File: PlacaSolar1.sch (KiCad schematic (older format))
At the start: 32 parts, among them J1 Jack-DC, J2 Conn_01x03_Female, J3 Conn_01x06_Female, J4 Conn_01x15_Female, J5 Conn_01x15_Female, SW1 SW_SPDT, SW2 SW_Push, U1 L78L05_SO8

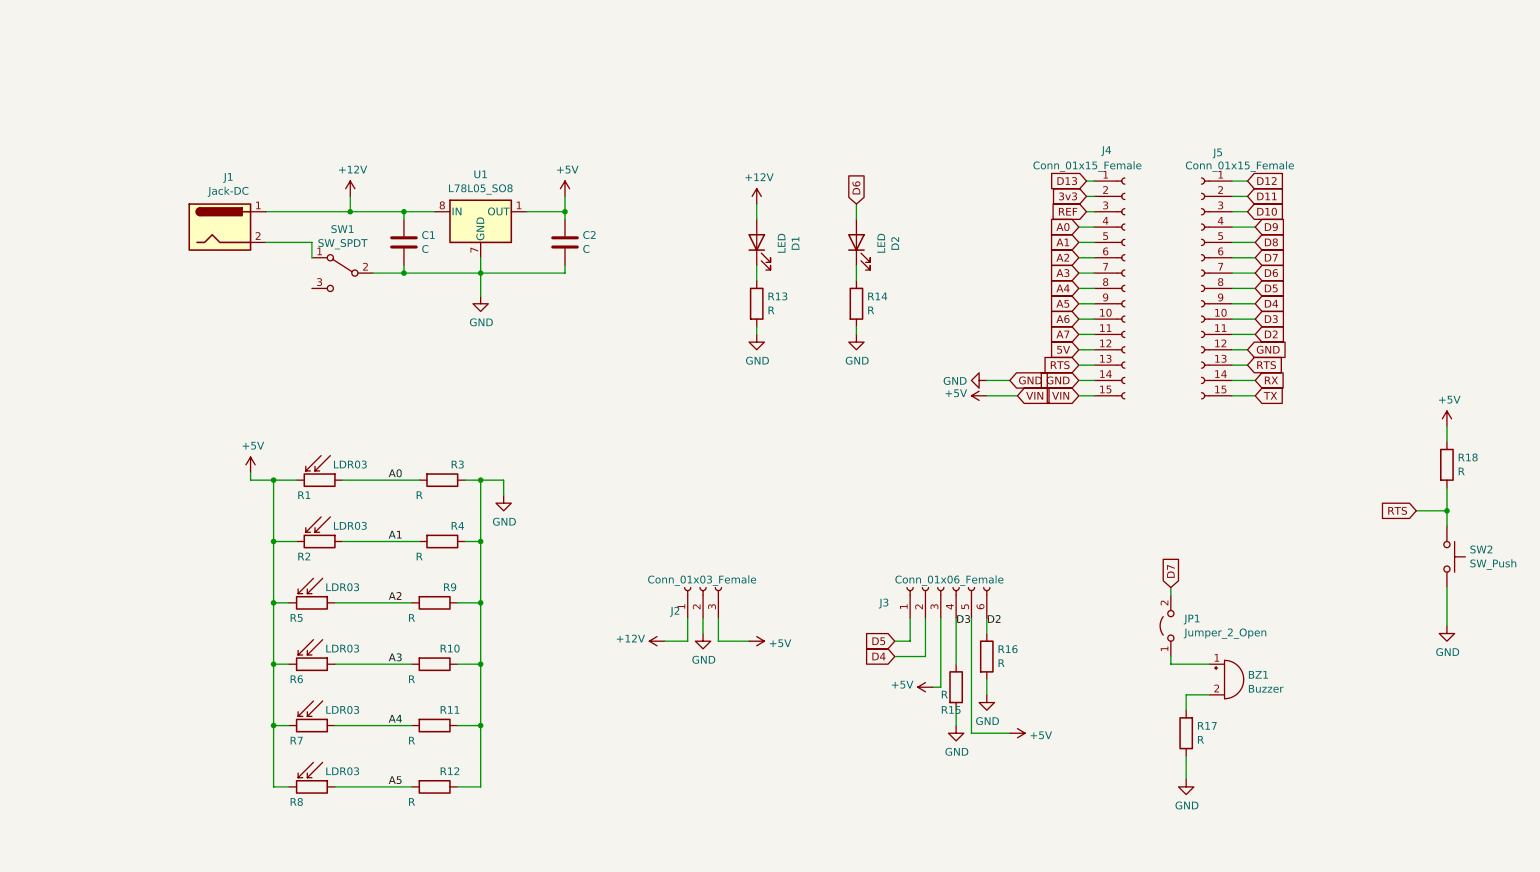
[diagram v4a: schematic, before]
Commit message: Corrigindo footprint do interruptor e adicionando alguns modelos 3d
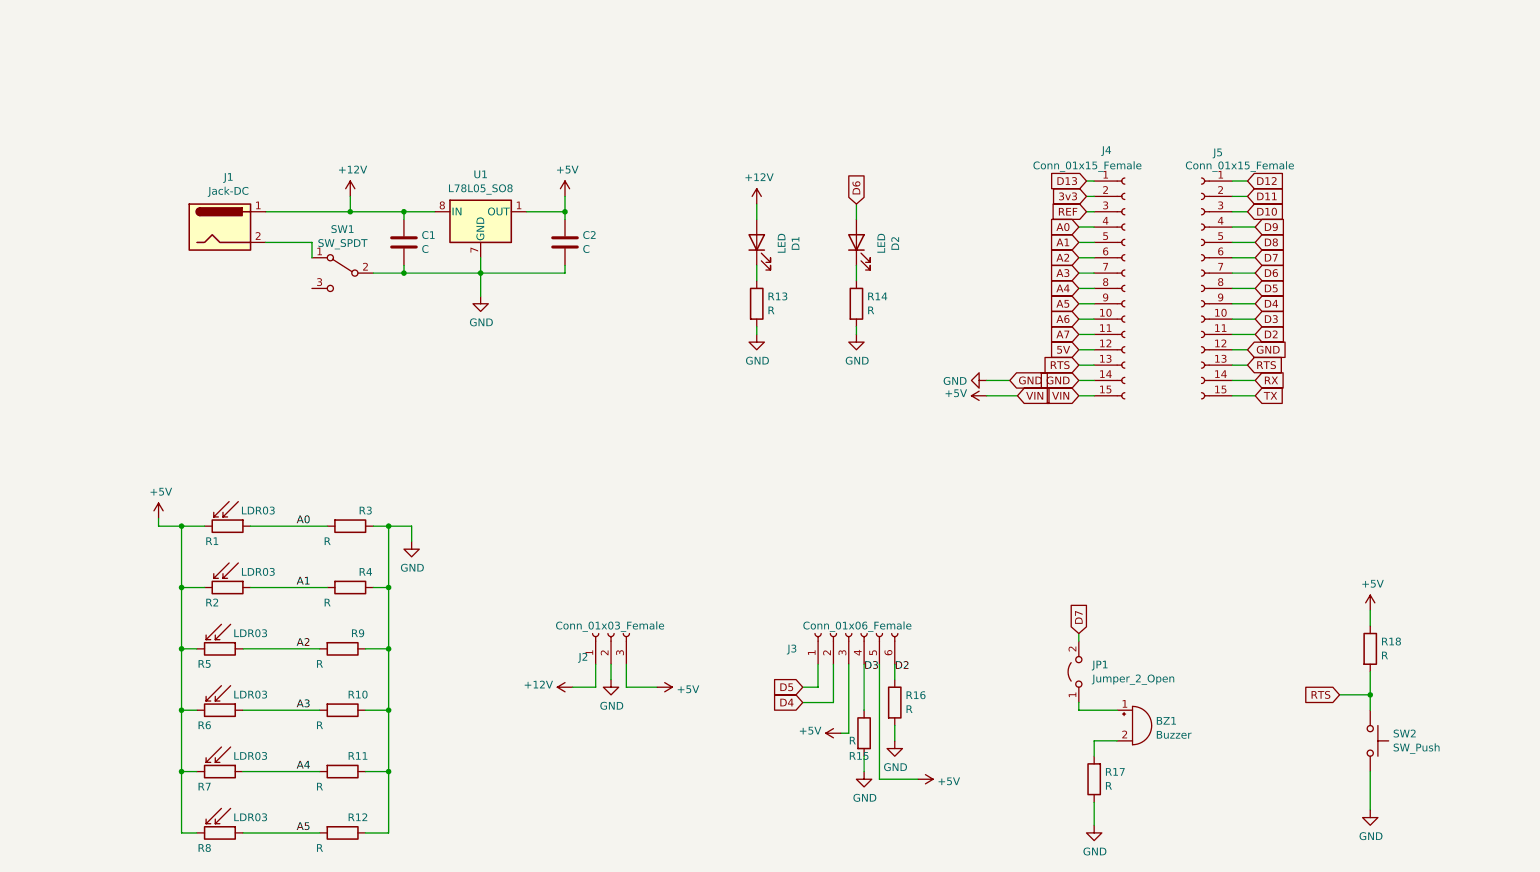
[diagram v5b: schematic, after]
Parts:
- SW1: footprint 2267077-2:TE_2267077-2 -> TE_2267077-2:TE_2267077-2
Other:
- moved on the sheet: BZ1, J2, J3, JP1, R1, R10, R11, R12, R15, R16, R17, R18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

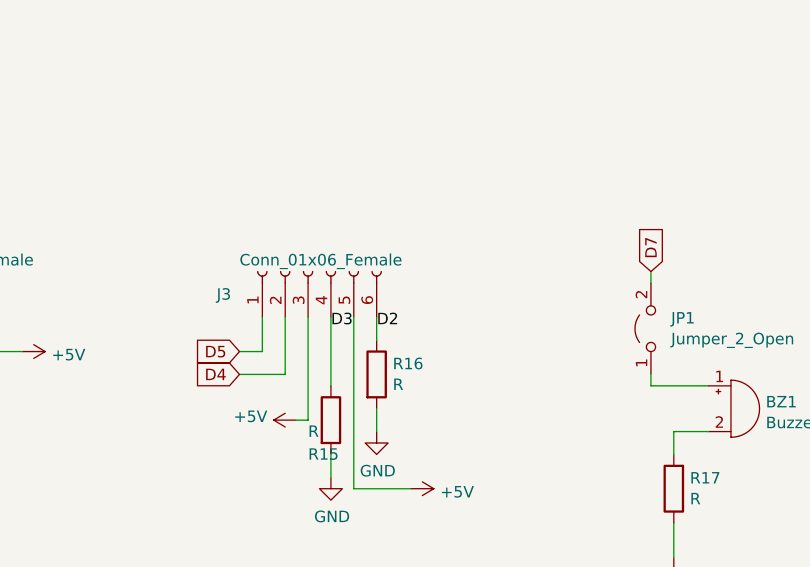
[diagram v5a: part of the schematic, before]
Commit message: Adicionando modelos 3d, falta o modelo dos bornes, inicio da PCB
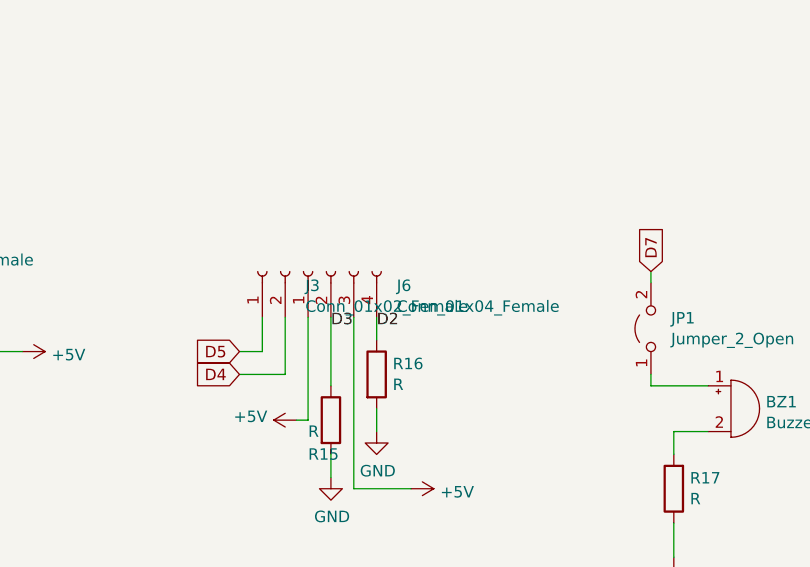
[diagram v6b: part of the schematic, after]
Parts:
- removed J3: Conn_01x06_Female, TerminalBlock:TerminalBlock_bornier-6_P5.08mm, symbol Connector:Conn_01x06_Female
- added J3: Conn_01x02_Female, TerminalBlock:TerminalBlock_bornier-2_P5.08mm, symbol Connector:Conn_01x02_Female
- added J6: Conn_01x04_Female, TerminalBlock:TerminalBlock_bornier-4_P5.08mm, symbol Connector:Conn_01x04_Female
- R2: footprint TerminalBlock:TerminalBlock_bornier-3_P5.08mm -> TerminalBlock:TerminalBlock_bornier-2_P5.08mm
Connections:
- net +5V: now also J6.1 (Pin_1), J6.3 (Pin_3)
- net D2: now also J6.4 (Pin_4)
- net D3: now also J6.2 (Pin_2)
- net D4: now also J3.2 (Pin_2)
- net D5: now also J3.1 (Pin_1)
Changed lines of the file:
@@
-	0    -1   -1   0
-$EndComp
-$Comp
-L Connector:Conn_01x06_Female J3
-U 1 1 61522486
-P 6150 4500
-F 0 "J3" V 6050 4900 50  0000 R CNN
-F 1 "Conn_01x06_Female" V 6200 4800 50  0000 R CNN
-F 2 "TerminalBlock:TerminalBlock_bornier-6_P5.08mm" H 6150 4500 50  0001 C CNN
-F 3 "~" H 6150 4500 50  0001 C CNN
-	1    6150 4500
 	0    -1   -1   0
 $EndComp
@@
 F 0 "R2" V 2200 4100 50  0000 C CNN
 F 1 "LDR03" V 2000 4400 50  0000 C CNN
-F 2 "TerminalBlock:TerminalBlock_bornier-3_P5.08mm" V 2275 4200 50  0001 C CNN
+F 2 "TerminalBlock:TerminalBlock_bornier-2_P5.08mm" V 2275 4200 50  0001 C CNN
 F 3 "http://www.elektronica-componenten.nl/WebRoot/StoreNL/Shops/61422969/54F1/BA0C/C664/31B9/2173/C0A8/2AB9/2AEF/LDR03IMP.pdf" H 2100 4150 50  0001 C CNN
 	1    2100 4200
@@
 Wire Wire Line
 	9550 4900 9550 4750
+$Comp
+L Connector:Conn_01x04_Female J6
+U 1 1 61473C9D
+P 6250 4500
+F 0 "J6" V 6188 4212 50  0000 R CNN
+F 1 "Conn_01x04_Female" V 6097 4212 50  0000 R CNN
+F 2 "TerminalBlock:TerminalBlock_bornier-4_P5.08mm" H 6250 4500 50  0001 C CNN
+F 3 "~" H 6250 4500 50  0001 C CNN
+	1    6250 4500
+	0    -1   -1   0
+$EndComp
+$Comp
+L Connector:Conn_01x02_Female J3
+U 1 1 61474DE5
+P 5950 4500
+F 0 "J3" V 5888 4312 50  0000 R CNN
+F 1 "Conn_01x02_Female" V 5797 4312 50  0000 R CNN
+F 2 "TerminalBlock:TerminalBlock_bornier-2_P5.08mm" H 5950 4500 50  0001 C CNN
+F 3 "~" H 5950 4500 50  0001 C CNN
+	1    5950 4500
+	0    -1   -1   0
+$EndComp
 $EndSCHEMATC

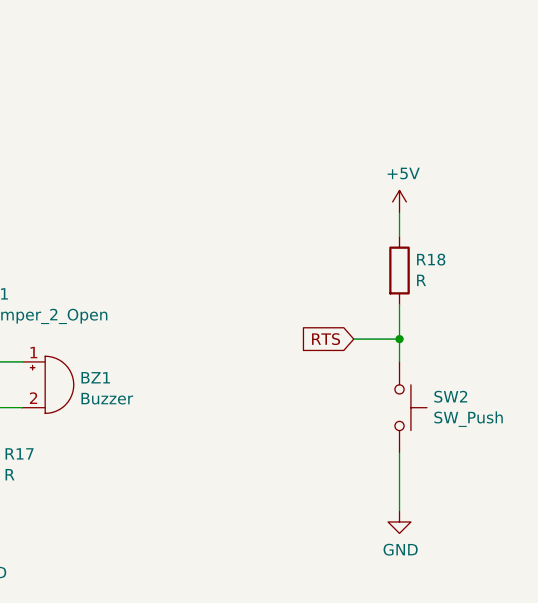
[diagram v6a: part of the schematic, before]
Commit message: Removendo botão de Reset
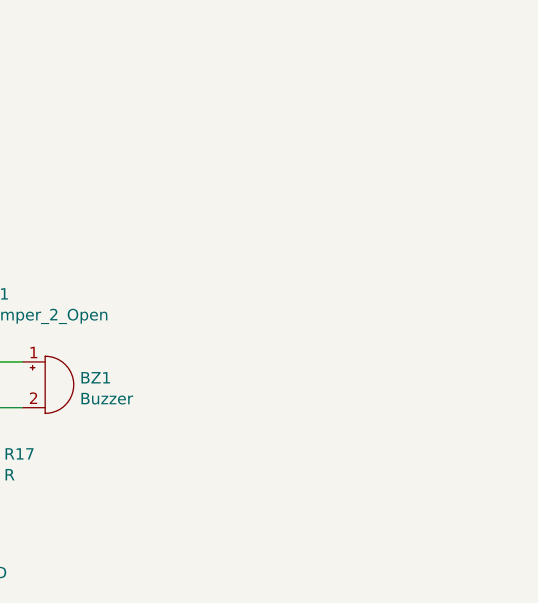
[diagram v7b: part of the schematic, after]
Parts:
- removed R18: R, Resistor_THT:R_Axial_DIN0207_L6.3mm_D2.5mm_P10.16mm_Horizontal, symbol Device:R
- removed SW2: SW_Push, Button_Switch_THT:SW_PUSH_6mm, symbol Switch:SW_Push
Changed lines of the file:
@@
 $EndComp
-$Comp
-L Switch:SW_Push SW2
-U 1 1 613C8742
-P 9550 5200
-F 0 "SW2" V 9504 5348 50  0000 L CNN
-F 1 "SW_Push" V 9595 5348 50  0000 L CNN
-F 2 "Button_Switch_THT:SW_PUSH_6mm" H 9550 5400 50  0001 C CNN
-F 3 "~" H 9550 5400 50  0001 C CNN
-	1    9550 5200
-	0    1    1    0
-$EndComp
-$Comp
-L power:+5V #PWR019
-U 1 1 613CCD35
-P 9550 4350
-F 0 "#PWR019" H 9550 4200 50  0001 C CNN
-F 1 "+5V" H 9565 4523 50  0000 C CNN
-F 2 "" H 9550 4350 50  0001 C CNN
-F 3 "" H 9550 4350 50  0001 C CNN
-	1    9550 4350
-	1    0    0    -1
-$EndComp
-$Comp
-L power:GND #PWR020
-U 1 1 613CD321
-P 9550 5650
-F 0 "#PWR020" H 9550 5400 50  0001 C CNN
-F 1 "GND" H 9555 5477 50  0000 C CNN
-F 2 "" H 9550 5650 50  0001 C CNN
-F 3 "" H 9550 5650 50  0001 C CNN
-	1    9550 5650
-	1    0    0    -1
-$EndComp
-$Comp
-L Device:R R18
-U 1 1 613D230B
-P 9550 4600
-F 0 "R18" H 9620 4646 50  0000 L CNN
-F 1 "R" H 9620 4555 50  0000 L CNN
-F 2 "Resistor_THT:R_Axial_DIN0207_L6.3mm_D2.5mm_P10.16mm_Horizontal" V 9480 4600 50  0001 C CNN
-F 3 "~" H 9550 4600 50  0001 C CNN
-	1    9550 4600
-	1    0    0    -1
-$EndComp
-Wire Wire Line
-	9550 5000 9550 4900
-Text GLabel 9350 4900 0    50   Input ~ 0
-RTS
-Wire Wire Line
-	9550 4450 9550 4350
-Wire Wire Line
-	9550 5400 9550 5650
-Wire Wire Line
-	9550 4900 9350 4900
-Connection ~ 9550 4900
-Wire Wire Line
-	9550 4900 9550 4750
 $Comp
 L Connector:Conn_01x04_Female J6

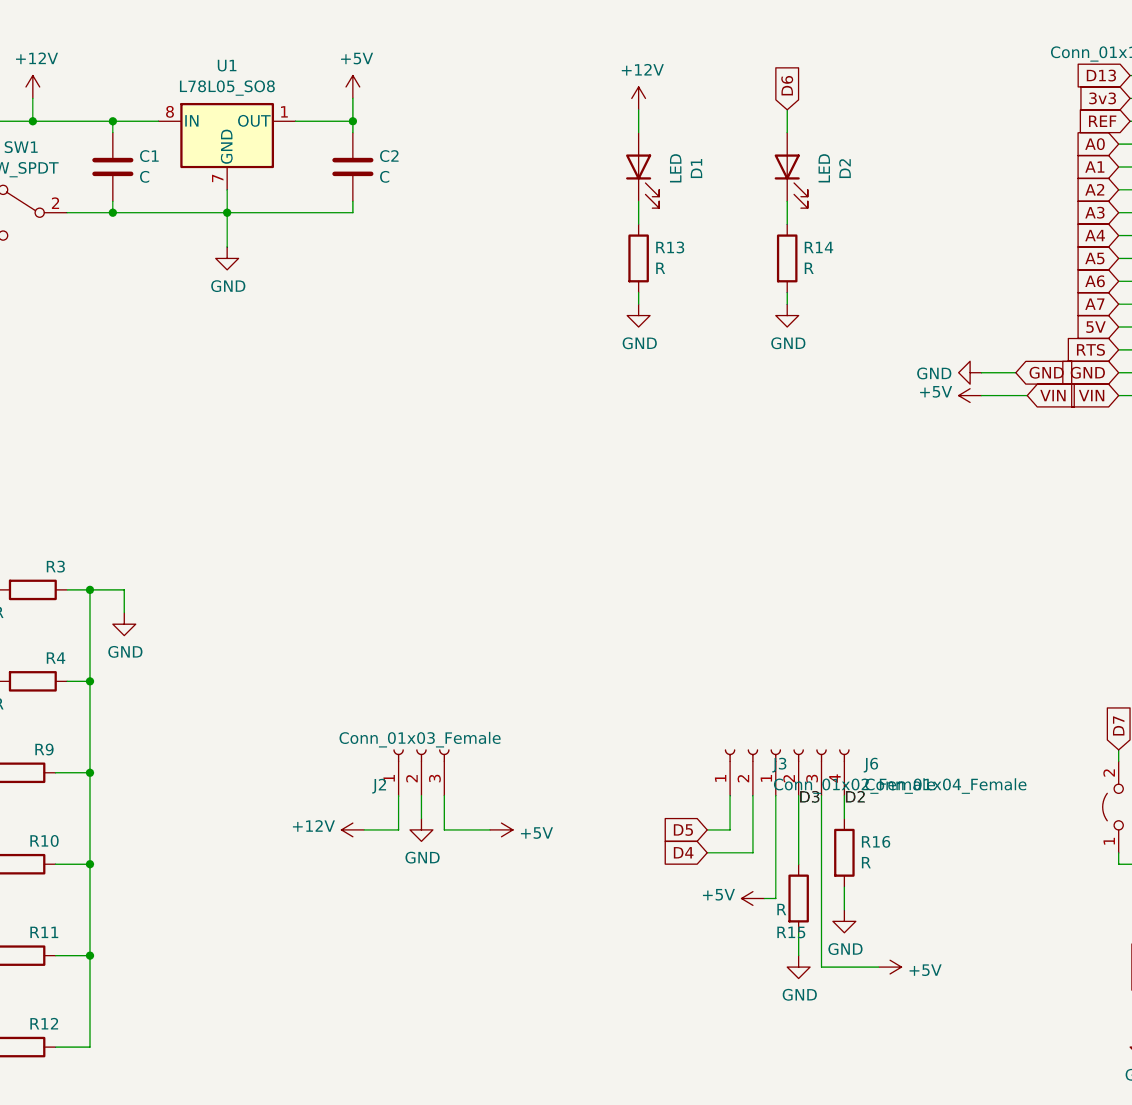
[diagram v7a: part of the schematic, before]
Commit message: Primeira versão de trilhas da PCB, falta verificar o tamanho de certos componentes
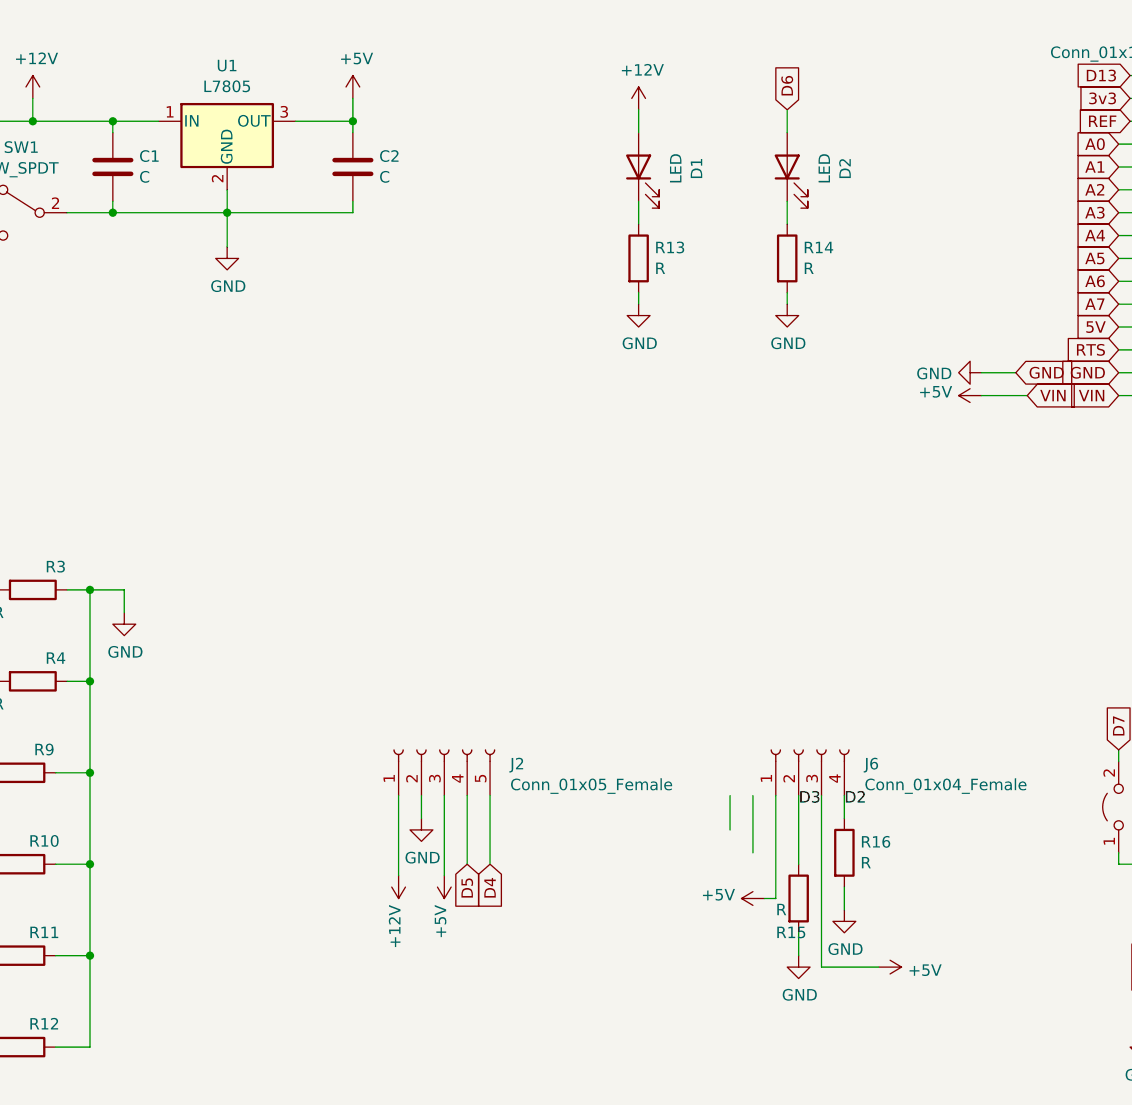
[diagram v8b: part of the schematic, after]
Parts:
- removed J2: Conn_01x03_Female, TerminalBlock:TerminalBlock_bornier-3_P5.08mm, symbol Connector:Conn_01x03_Female
- removed J3: Conn_01x02_Female, TerminalBlock:TerminalBlock_bornier-2_P5.08mm, symbol Connector:Conn_01x02_Female
- removed U1: L78L05_SO8, Package_TO_SOT_THT:TO-220-3_Vertical, symbol Regulator_Linear:L78L05_SO8
- added J2: Conn_01x05_Female, Connector_PinHeader_2.54mm:PinHeader_1x05_P2.54mm_Vertical, symbol Connector:Conn_01x05_Female
- added U1: L7805, Package_TO_SOT_THT:TO-220-3_Vertical, symbol Regulator_Linear:L7805
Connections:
- wire segments 110 -> 108
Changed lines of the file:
@@
-	1    0    0    -1
-$EndComp
-$Comp
-L Regulator_Linear:L78L05_SO8 U1
-U 1 1 613A917B
-P 3750 1750
-F 0 "U1" H 3750 1992 50  0000 C CNN
-F 1 "L78L05_SO8" H 3750 1901 50  0000 C CNN
-F 2 "Package_TO_SOT_THT:TO-220-3_Vertical" H 3850 1950 50  0001 C CIN
-F 3 "http://www.st.com/content/ccc/resource/technical/document/datasheet/15/55/e5/aa/23/5b/43/fd/CD00000446.pdf/files/CD00000446.pdf/jcr:content/translations/en.CD00000446.pdf" H 3950 1750 50  0001 C CNN
-	1    3750 1750
 	1    0    0    -1
 $EndComp
@@
 	6050 4700 6050 4950
 Wire Wire Line
-	5850 4950 6050 4950
-Wire Wire Line
 	5950 4700 5950 4850
-Wire Wire Line
-	5850 4850 5950 4850
-Text GLabel 5850 4950 0    50   Input ~ 0
+Text GLabel 4900 5000 3    50   Input ~ 0
 D4
-Text GLabel 5850 4850 0    50   Input ~ 0
+Text GLabel 4800 5000 3    50   Input ~ 0
 D5
-$Comp
-L Connector:Conn_01x03_Female J2
-U 1 1 613F1034
-P 4600 4500
-F 0 "J2" V 4446 4648 50  0000 L CNN
-F 1 "Conn_01x03_Female" V 4650 4150 50  0000 L CNN
-F 2 "TerminalBlock:TerminalBlock_bornier-3_P5.08mm" H 4600 4500 50  0001 C CNN
-F 3 "~" H 4600 4500 50  0001 C CNN
-	1    4600 4500
-	0    -1   -1   0
-$EndComp
 $Comp
 L power:GND #PWR07
@@
 	1    0    0    -1
 $EndComp
-Wire Wire Line
-	4600 4800 4600 4700
 $Comp
 L power:+12V #PWR06
 U 1 1 613F8720
-P 4350 4850
-F 0 "#PWR06" H 4350 4700 50  0001 C CNN
-F 1 "+12V" V 4365 4978 50  0000 L CNN
-F 2 "" H 4350 4850 50  0001 C CNN
-F 3 "" H 4350 4850 50  0001 C CNN
-	1    4350 4850
-	0    -1   -1   0
-$EndComp
-Wire Wire Line
-	4500 4700 4500 4850
-Wire Wire Line
-	4500 4850 4350 4850
+P 4500 5050
+F 0 "#PWR06" H 4500 4900 50  0001 C CNN
+F 1 "+12V" V 4515 5178 50  0000 L CNN
+F 2 "" H 4500 5050 50  0001 C CNN
+F 3 "" H 4500 5050 50  0001 C CNN
+	1    4500 5050
+	-1   0    0    1
+$EndComp
 $Comp
 L power:+5V #PWR08
 U 1 1 613FB42D
-P 4900 4850
-F 0 "#PWR08" H 4900 4700 50  0001 C CNN
-F 1 "+5V" V 4915 4978 50  0000 L CNN
-F 2 "" H 4900 4850 50  0001 C CNN
-F 3 "" H 4900 4850 50  0001 C CNN
-	1    4900 4850
-	0    1    1    0
-$EndComp
-Wire Wire Line
-	4900 4850 4700 4850
-Wire Wire Line
-	4700 4850 4700 4700
+P 4700 5050
+F 0 "#PWR08" H 4700 4900 50  0001 C CNN
+F 1 "+5V" V 4715 5178 50  0000 L CNN
+F 2 "" H 4700 5050 50  0001 C CNN
+F 3 "" H 4700 5050 50  0001 C CNN
+	1    4700 5050
+	-1   0    0    1
+$EndComp
 $Comp
 L Sensor_Optical:LDR03 R1
@@
 	0    -1   -1   0
 $EndComp
-$Comp
-L Connector:Conn_01x02_Female J3
-U 1 1 61474DE5
-P 5950 4500
-F 0 "J3" V 5888 4312 50  0000 R CNN
-F 1 "Conn_01x02_Female" V 5797 4312 50  0000 R CNN
-F 2 "TerminalBlock:TerminalBlock_bornier-2_P5.08mm" H 5950 4500 50  0001 C CNN
-F 3 "~" H 5950 4500 50  0001 C CNN
-	1    5950 4500
+Wire Wire Line
+	4600 4800 4600 4700
+$Comp
+L Connector:Conn_01x05_Female J2
+U 1 1 61425088
+P 4700 4500
+F 0 "J2" V 4638 4212 50  0000 R CNN
+F 1 "Conn_01x05_Female" V 4547 4212 50  0000 R CNN
+F 2 "Connector_PinHeader_2.54mm:PinHeader_1x05_P2.54mm_Vertical" H 4700 4500 50  0001 C CNN
+F 3 "~" H 4700 4500 50  0001 C CNN
+	1    4700 4500
 	0    -1   -1   0
 $EndComp
+Wire Wire Line
+	4700 4700 4700 5050
+Wire Wire Line
+	4500 4700 4500 5050
+Wire Wire Line
+	4800 5000 4800 4700
+Wire Wire Line
+	4900 5000 4900 4700
+$Comp
+L Regulator_Linear:L7805 U1
+U 1 1 6147A2C6
+P 3750 1750
+F 0 "U1" H 3750 1992 50  0000 C CNN
+F 1 "L7805" H 3750 1901 50  0000 C CNN
+F 2 "Package_TO_SOT_THT:TO-220-3_Vertical" H 3775 1600 50  0001 L CIN
+F 3 "http://www.st.com/content/ccc/resource/technical/document/datasheet/41/4f/b3/b0/12/d4/47/88/CD00000444.pdf/files/CD00000444.pdf/jcr:content/translations/en.CD00000444.pdf" H 3750 1700 50  0001 C CNN
+	1    3750 1750
+	1    0    0    -1
+$EndComp
 $EndSCHEMATC
